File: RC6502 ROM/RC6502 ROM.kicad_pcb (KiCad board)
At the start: 2 copper layers, 99.1 x 54.6 mm, 13 parts, among them J1 CONN_01X39, U1 28C256, U2 74HCT00, U3 74HCT00

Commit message: Exported files
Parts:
- moved C2 2.54 mm to (111.8, 102.9)
- moved U2 2.54 mm to (119.4, 109.2)
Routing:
- net A13: track 117.0 -> 121.4 mm
- net Net-(U2-Pad3): track 25.7 -> 23.2 mm
- net A15: track 131.8 -> 133.0 mm
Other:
- board text added: "Address A0 - A15"
- board text added: "Data D7 - D0"
- board text added: "GND"
- board text added: "Page"
- board text added: "Pin 1"
- board text added: "RC6502 ROM Revision A"
- board text added: "VCC"

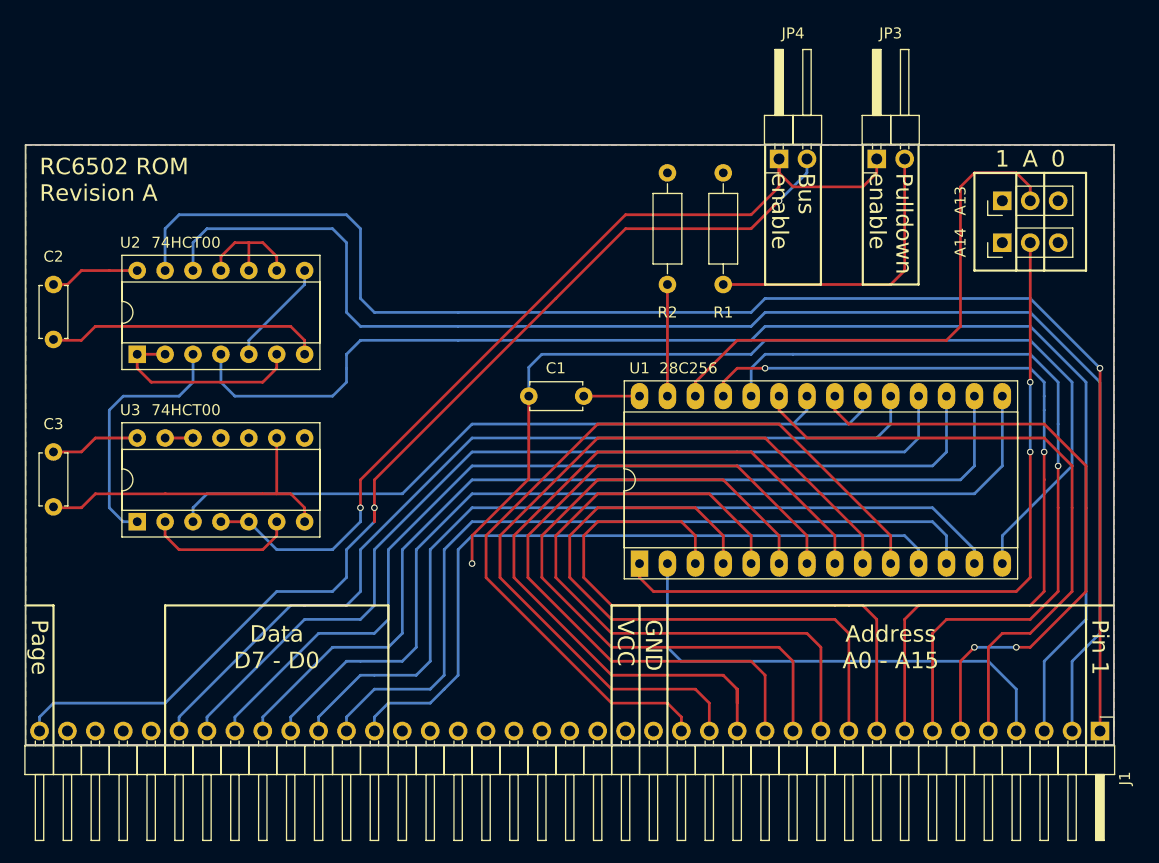
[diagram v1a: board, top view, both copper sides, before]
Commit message: Added jumper select to decide if paging hardware installed
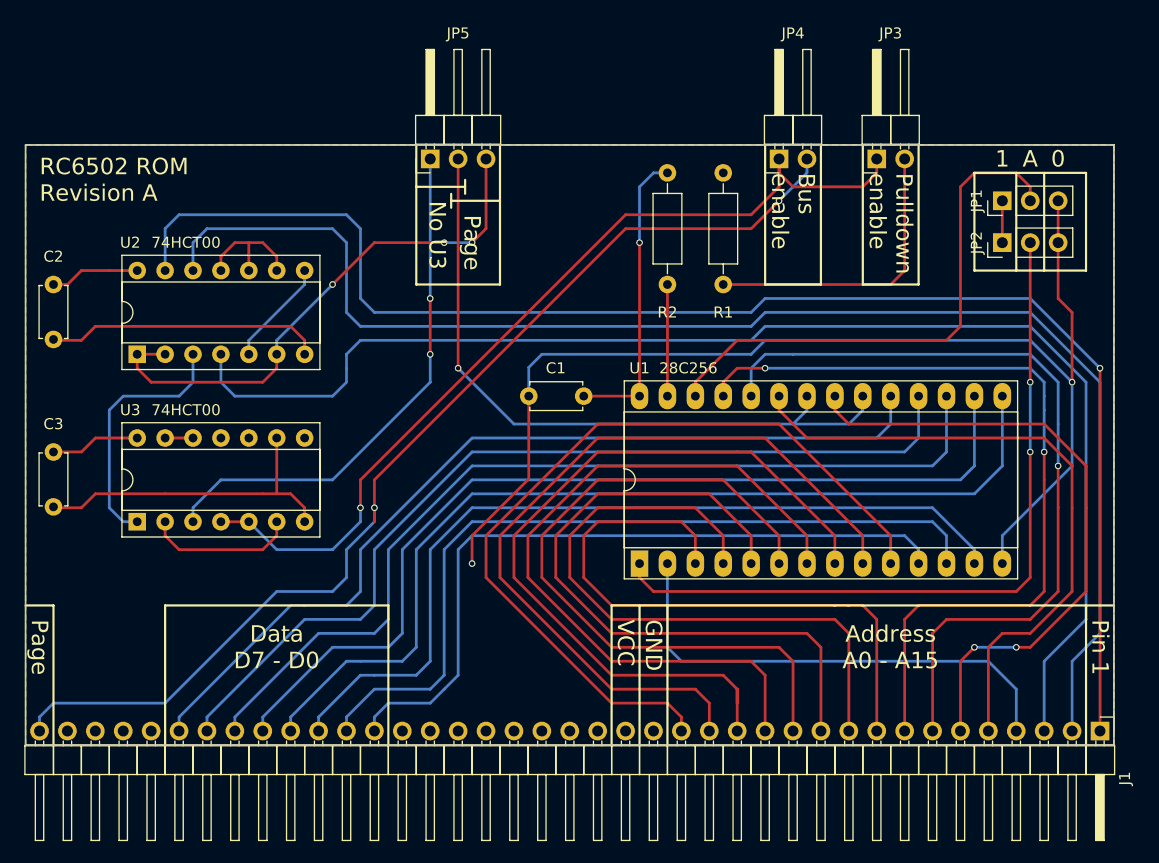
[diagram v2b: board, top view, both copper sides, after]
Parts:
- removed A13: A13 Select, Pin_Headers:Pin_Header_Straight_1x03_Pitch2.54mm
- removed A14: A14 Select, Pin_Headers:Pin_Header_Straight_1x03_Pitch2.54mm
- added JP1: A13 Select, Pin_Headers:Pin_Header_Straight_1x03_Pitch2.54mm, F.Cu at (198.1, 95.2)
- added JP2: A14 Select, Pin_Headers:Pin_Header_Straight_1x03_Pitch2.54mm, F.Cu at (198.1, 99.1)
- added JP5: Page mode, Pin_Headers:Pin_Header_Angled_1x03_Pitch2.54mm, F.Cu at (146.1, 91.4)
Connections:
- U3 pad 3: CS -> Net-(JP5-Pad1)
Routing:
- net Net-(JP5-Pad1): track 0.00 -> 47.9 mm, vias 0 -> 2
- net CS_IN: track 18.8 -> 49.7 mm, vias 0 -> 3
- net VCC: track 21.4 -> 47.3 mm, vias 0 -> 1
- net GND: track 149.2 -> 166.3 mm, vias 1 -> 2
- net CS: track 70.2 -> 62.8 mm, vias 0 -> 1
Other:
- board text added: "No U3"

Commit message: ROM revision B
JP5 inside U3 footprint is used to designate wether paging hardware is installed or not (skip  C3 and U3).
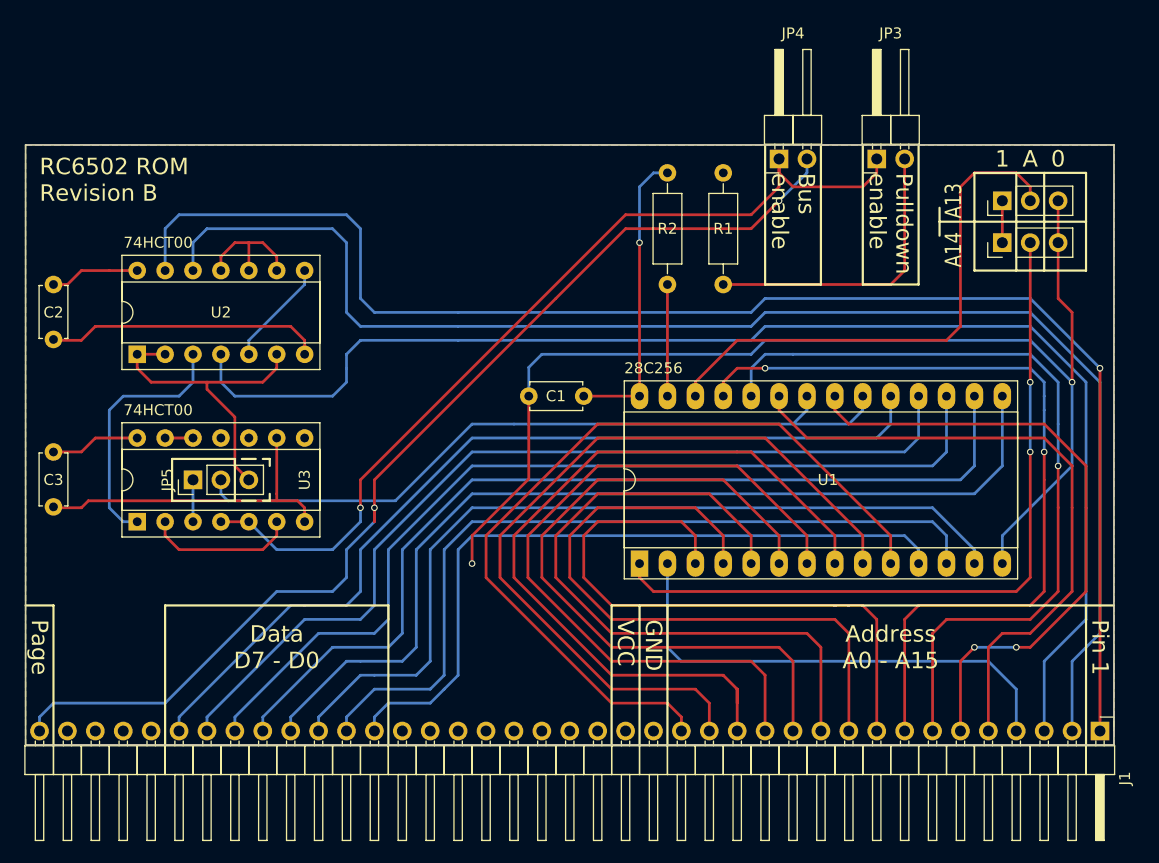
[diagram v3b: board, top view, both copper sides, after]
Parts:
- JP5: footprint Pin_Headers:Pin_Header_Angled_1x03_Pitch2.54mm -> Pin_Headers:Pin_Header_Straight_1x03_Pitch2.54mm
- moved JP5 36.3 mm to (124.5, 120.7)
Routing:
- net Net-(JP5-Pad1): track 47.9 -> 3.81 mm, vias 2 -> 0
- net CS_IN: track 49.7 -> 29.3 mm, vias 3 -> 0
- net CS: track 62.8 -> 67.7 mm, vias 1 -> 0
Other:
- board text added: "A13"
- board text added: "A14"
- board text added: "RC6502 ROM Revision B"
- board text removed: "No U3"
- board text removed: "RC6502 ROM Revision A"

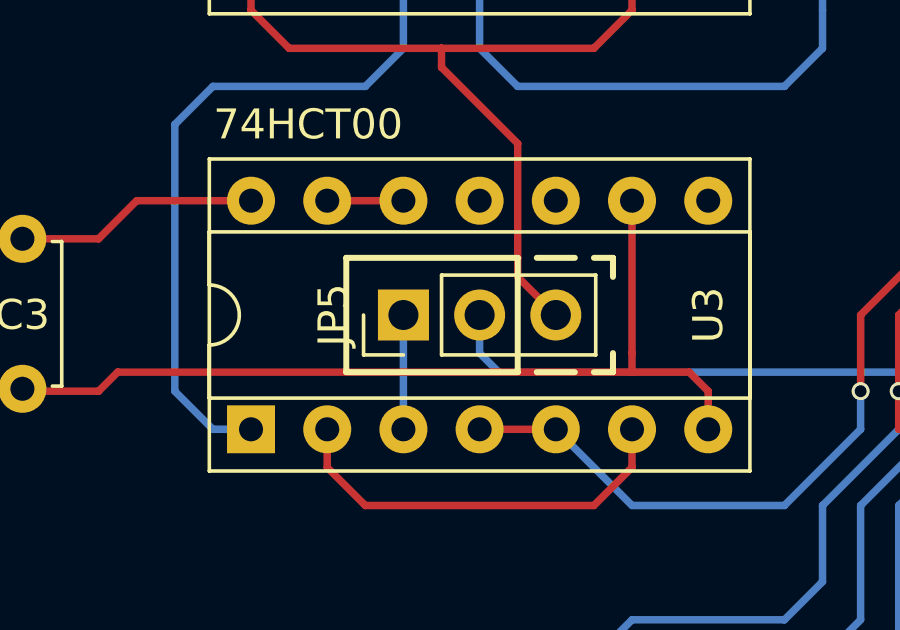
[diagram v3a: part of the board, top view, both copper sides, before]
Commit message: Moved JP5 pins to back of board, only want to solder wire across it and not actually mount pins.
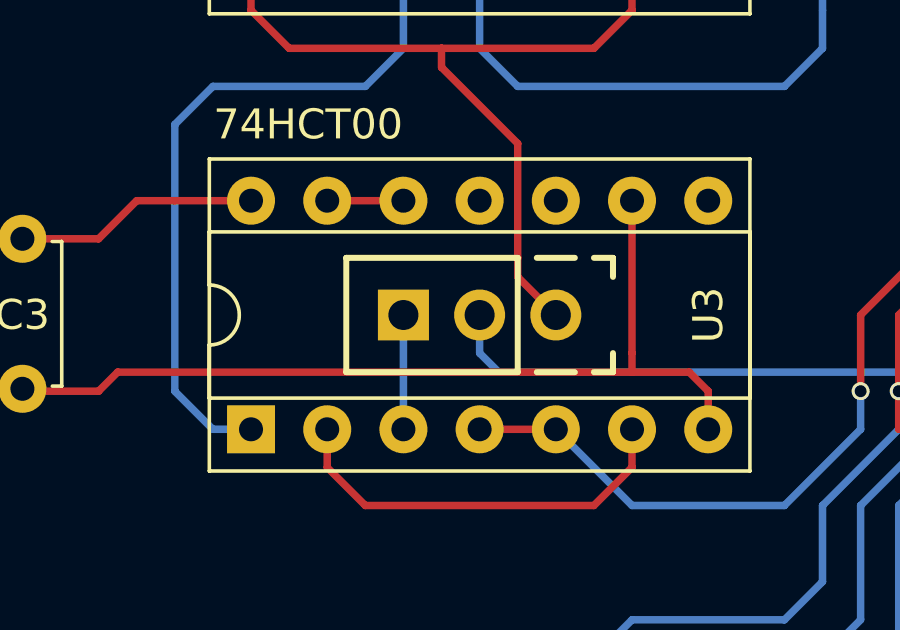
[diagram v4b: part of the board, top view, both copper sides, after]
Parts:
- JP5: moved to B.Cu
- turned JP5 to 270 degrees
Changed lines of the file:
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@@
     )
   )
-  (module Pin_Headers:Pin_Header_Straight_1x03_Pitch2.54mm (layer F.Cu)
-    (at 124.46 120.65 90)
+  (module Pin_Headers:Pin_Header_Straight_1x03_Pitch2.54mm (layer B.Cu)
+    (at 124.46 120.65 270)
     (descr "Through hole straight pin header, 1x03, 2.54mm pitch, single row")
     (tags "Through hole pin header THT 1x03 2.54mm single row")
-    (fp_text reference JP5 (at 0 -2.33 90) (layer F.SilkS)
-      (effects (font (size 1 1) (thickness 0.15)))
+    (fp_text reference JP5 (at 0 2.33 270) (layer B.SilkS)
+      (effects (font (size 1 1) (thickness 0.15)) (justify mirror))
     )
-    (fp_text value "Page mode" (at 0 7.41 90) (layer F.Fab)
-      (effects (font (size 1 1) (thickness 0.15)))
+    (fp_text value "Page mode" (at 0 -7.41 270) (layer B.Fab)
+      (effects (font (size 1 1) (thickness 0.15)) (justify mirror))
     )
-    (fp_line (start -1.27 -1.27) (end -1.27 6.35) (layer F.Fab) (width 0.1))
-    (fp_line (start -1.27 6.35) (end 1.27 6.35) (layer F.Fab) (width 0.1))
-    (fp_line (start 1.27 6.35) (end 1.27 -1.27) (layer F.Fab) (width 0.1))
-    (fp_line (start 1.27 -1.27) (end -1.27 -1.27) (layer F.Fab) (width 0.1))
-    (fp_line (start -1.33 1.27) (end -1.33 6.41) (layer F.SilkS) (width 0.12))
-    (fp_line (start -1.33 6.41) (end 1.33 6.41) (layer F.SilkS) (width 0.12))
-    (fp_line (start 1.33 6.41) (end 1.33 1.27) (layer F.SilkS) (width 0.12))
-    (fp_line (start 1.33 1.27) (end -1.33 1.27) (layer F.SilkS) (width 0.12))
-    (fp_line (start -1.33 0) (end -1.33 -1.33) (layer F.SilkS) (width 0.12))
-    (fp_line (start -1.33 -1.33) (end 0 -1.33) (layer F.SilkS) (width 0.12))
-    (fp_line (start -1.8 -1.8) (end -1.8 6.85) (layer F.CrtYd) (width 0.05))
-    (fp_line (start -1.8 6.85) (end 1.8 6.85) (layer F.CrtYd) (width 0.05))
-    (fp_line (start 1.8 6.85) (end 1.8 -1.8) (layer F.CrtYd) (width 0.05))
-    (fp_line (start 1.8 -1.8) (end -1.8 -1.8) (layer F.CrtYd) (width 0.05))
-    (fp_text user %R (at 0 -2.33 90) (layer F.Fab)
-      (effects (font (size 1 1) (thickness 0.15)))
+    (fp_line (start -1.27 1.27) (end -1.27 -6.35) (layer B.Fab) (width 0.1))
+    (fp_line (start -1.27 -6.35) (end 1.27 -6.35) (layer B.Fab) (width 0.1))
+    (fp_line (start 1.27 -6.35) (end 1.27 1.27) (layer B.Fab) (width 0.1))
+    (fp_line (start 1.27 1.27) (end -1.27 1.27) (layer B.Fab) (width 0.1))
+    (fp_line (start -1.33 -1.27) (end -1.33 -6.41) (layer B.SilkS) (width 0.12))
+    (fp_line (start -1.33 -6.41) (end 1.33 -6.41) (layer B.SilkS) (width 0.12))
+    (fp_line (start 1.33 -6.41) (end 1.33 -1.27) (layer B.SilkS) (width 0.12))
+    (fp_line (start 1.33 -1.27) (end -1.33 -1.27) (layer B.SilkS) (width 0.12))
+    (fp_line (start -1.33 0) (end -1.33 1.33) (layer B.SilkS) (width 0.12))
+    (fp_line (start -1.33 1.33) (end 0 1.33) (layer B.SilkS) (width 0.12))
+    (fp_line (start -1.8 1.8) (end -1.8 -6.85) (layer B.CrtYd) (width 0.05))
+    (fp_line (start -1.8 -6.85) (end 1.8 -6.85) (layer B.CrtYd) (width 0.05))
+    (fp_line (start 1.8 -6.85) (end 1.8 1.8) (layer B.CrtYd) (width 0.05))
+    (fp_line (start 1.8 1.8) (end -1.8 1.8) (layer B.CrtYd) (width 0.05))
+    (fp_text user %R (at 0 2.33 270) (layer B.Fab)
+      (effects (font (size 1 1) (thickness 0.15)) (justify mirror))
     )
-    (pad 1 thru_hole rect (at 0 0 90) (size 1.7 1.7) (drill 1) (layers *.Cu *.Mask)
+    (pad 1 thru_hole rect (at 0 0 270) (size 1.7 1.7) (drill 1) (layers *.Cu *.Mask)
       (net 39 "Net-(JP5-Pad1)"))
-    (pad 2 thru_hole oval (at 0 2.54 90) (size 1.7 1.7) (drill 1) (layers *.Cu *.Mask)
+    (pad 2 thru_hole oval (at 0 -2.54 270) (size 1.7 1.7) (drill 1) (layers *.Cu *.Mask)
       (net 32 CS))
-    (pad 3 thru_hole oval (at 0 5.08 90) (size 1.7 1.7) (drill 1) (layers *.Cu *.Mask)
+    (pad 3 thru_hole oval (at 0 -5.08 270) (size 1.7 1.7) (drill 1) (layers *.Cu *.Mask)
       (net 33 CS_IN))
     (model ${KISYS3DMOD}/Pin_Headers.3dshapes/Pin_Header_Straight_1x03_Pitch2.54mm.wrl
@@
   (segment (start 149.86 115.57) (end 153.67 115.57) (width 0.25) (layer B.Cu) (net 32))
   (segment (start 179.07 115.57) (end 153.67 115.57) (width 0.25) (layer B.Cu) (net 32))
-  (segment (start 127 121.92) (end 127 120.65) (width 0.25) (layer B.Cu) (net 32) (status 800000))
+  (segment (start 127 121.92) (end 127 120.65) (width 0.25) (layer B.Cu) (net 32))
   (segment (start 127.635 122.555) (end 127 121.92) (width 0.25) (layer B.Cu) (net 32))
   (segment (start 185.42 113.03) (end 185.42 114.3) (width 0.25) (layer B.Cu) (net 32))
@@
   (segment (start 128.27 114.935) (end 128.27 118.745) (width 0.25) (layer F.Cu) (net 33))
   (segment (start 125.73 111.76) (end 125.73 112.395) (width 0.25) (layer F.Cu) (net 33))
-  (segment (start 128.27 119.38) (end 129.54 120.65) (width 0.25) (layer F.Cu) (net 33) (status 800000))
+  (segment (start 128.27 119.38) (end 129.54 120.65) (width 0.25) (layer F.Cu) (net 33))
   (segment (start 121.92 109.22) (end 119.38 109.22) (width 0.25) (layer F.Cu) (net 33))
   (segment (start 132.08 109.22) (end 132.08 110.49) (width 0.25) (layer F.Cu) (net 33))
@@
   (segment (start 132.08 125.73) (end 130.81 127) (width 0.25) (layer F.Cu) (net 37))
   (segment (start 167.64 113.03) (end 167.64 102.87) (width 0.25) (layer F.Cu) (net 38))
-  (segment (start 124.46 124.46) (end 124.46 120.65) (width 0.25) (layer B.Cu) (net 39) (status C00000))
+  (segment (start 124.46 124.46) (end 124.46 120.65) (width 0.25) (layer B.Cu) (net 39))
   (zone (net 2) (net_name GND) (layer B.Cu) (hatch edge 0.508)
     (connect_pads (clearance 0.508))
